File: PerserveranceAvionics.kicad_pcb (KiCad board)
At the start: 4 copper layers, 19 parts, among them J11 ADA-SD READ/WRITE, J4 Batt_Vin

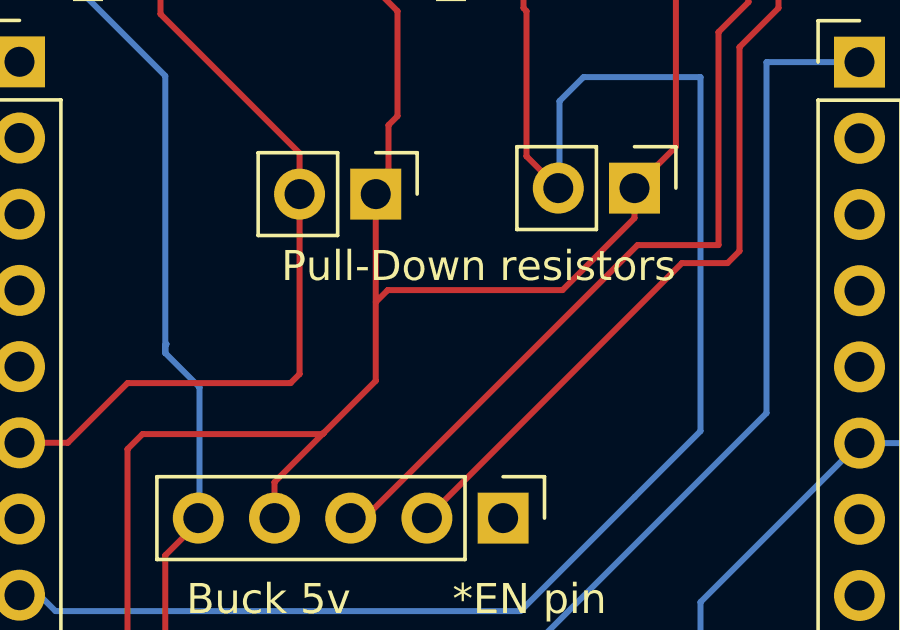
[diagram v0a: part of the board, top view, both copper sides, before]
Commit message: added through-hole resistor values, documented title & sensor specs
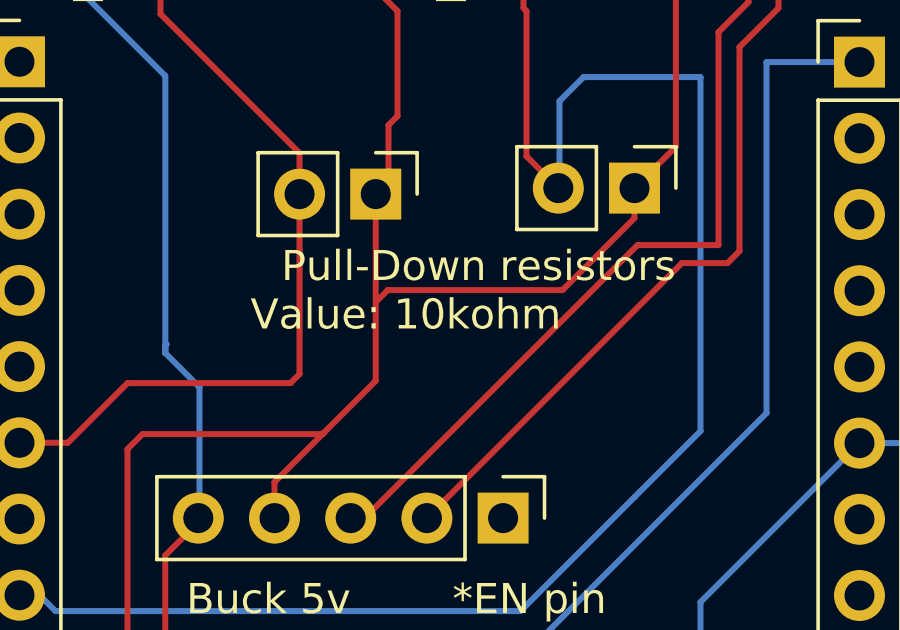
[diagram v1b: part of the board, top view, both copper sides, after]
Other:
- board text added: "Property of Hornet Aerospace & Propulsion RSO of California State University, Sacramento & College of Engineering and Computer Science circa 2025"
- board text added: "Sensor Index: ICM 20948 Adafruit Breakout : 9DOF IMU BMP 390 Adafruit Breakout : Barometric Pressure Sensor accurate within =>1m ADXL 375 Adafruit Breakout : 3DOF accelerometer, measures up to 200 G's"
- board text added: "Value: 10kohm"
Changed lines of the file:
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@@
+		)
+	)
+	(gr_text "Value: 10kohm "
+		(at 94.9 42.4 0)
+		(layer "F.SilkS")
+		(effects
+			(font
+				(size 1 1)
+				(thickness 0.125)
+			)
+			(justify left bottom)
 		)
 	)
@@
 		)
 	)
+	(gr_text "Property of Hornet Aerospace & Propulsion \n\nRSO of California State University, Sacramento \n& College of Engineering and Computer Science \n\ncirca 2025 "
+		(at 119.8 101 270)
+		(layer "B.SilkS")
+		(effects
+			(font
+				(size 1.5 1.5)
+				(thickness 0.3)
+				(bold yes)
+			)
+			(justify left bottom mirror)
+		)
+	)
+	(gr_text "Sensor Index: \n\nICM 20948 Adafruit Breakout : 9DOF IMU \nBMP 390   Adafruit Breakout : Barometric Pressure Sensor accurate within =>1m   \nADXL 375  Adafruit Breakout : 3DOF accelerometer, measures up to 200 G's\n\n\n"
+		(at 87.1 98.9 270)
+		(layer "B.SilkS")
+		(effects
+			(font
+				(size 1.1 1.1)
+				(thickness 0.275)
+				(bold yes)
+			)
+			(justify left bottom mirror)
+		)
+	)
